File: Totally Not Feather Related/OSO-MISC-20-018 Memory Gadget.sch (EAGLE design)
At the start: 57 parts, among them IC1 LS013B4DN04, IC2 S-882150APH, IC3 ATSAMD21G18_QFN, J2 10118193-0001LF, J4 SM04B-SRSS-TB(LF)(SN), Q1 DMG341, SW1 JS102011SAQN, SW2 SPST_TACT-KMR2, U1 MCP73831T-2ACI/OT, U2 AP2112K-3.3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

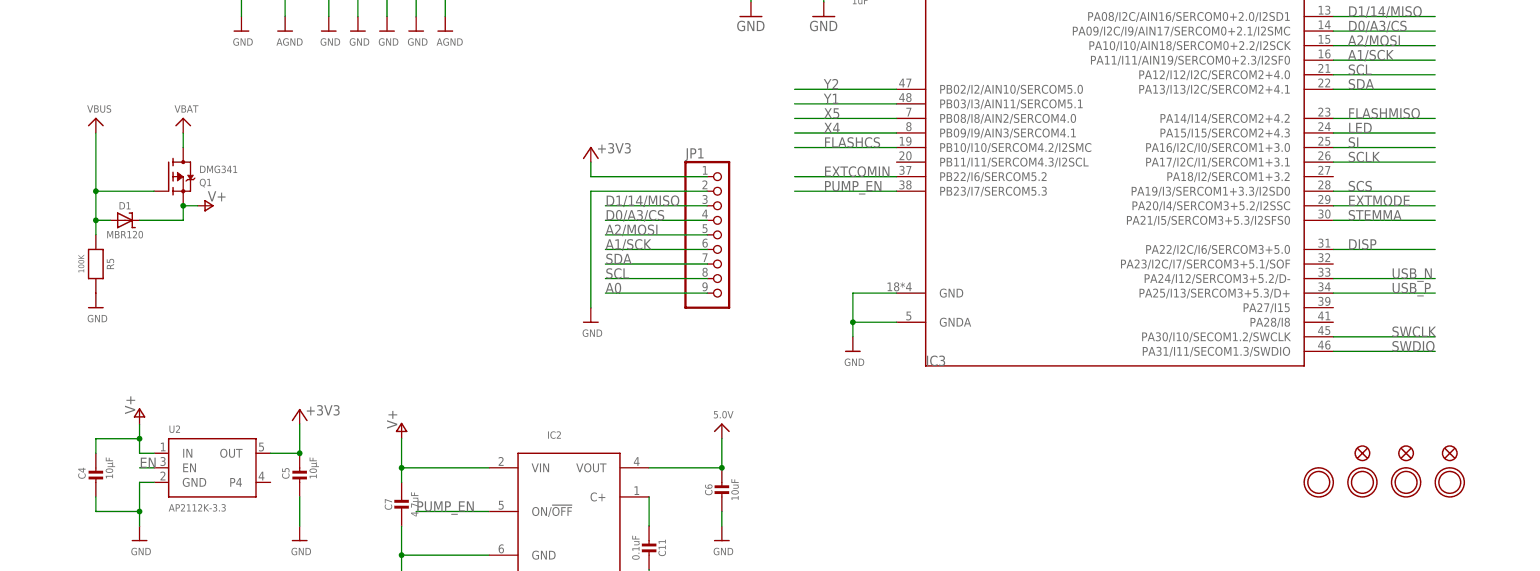
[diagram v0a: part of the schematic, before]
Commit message: add EN pull-up, fix SPI flash pin selection
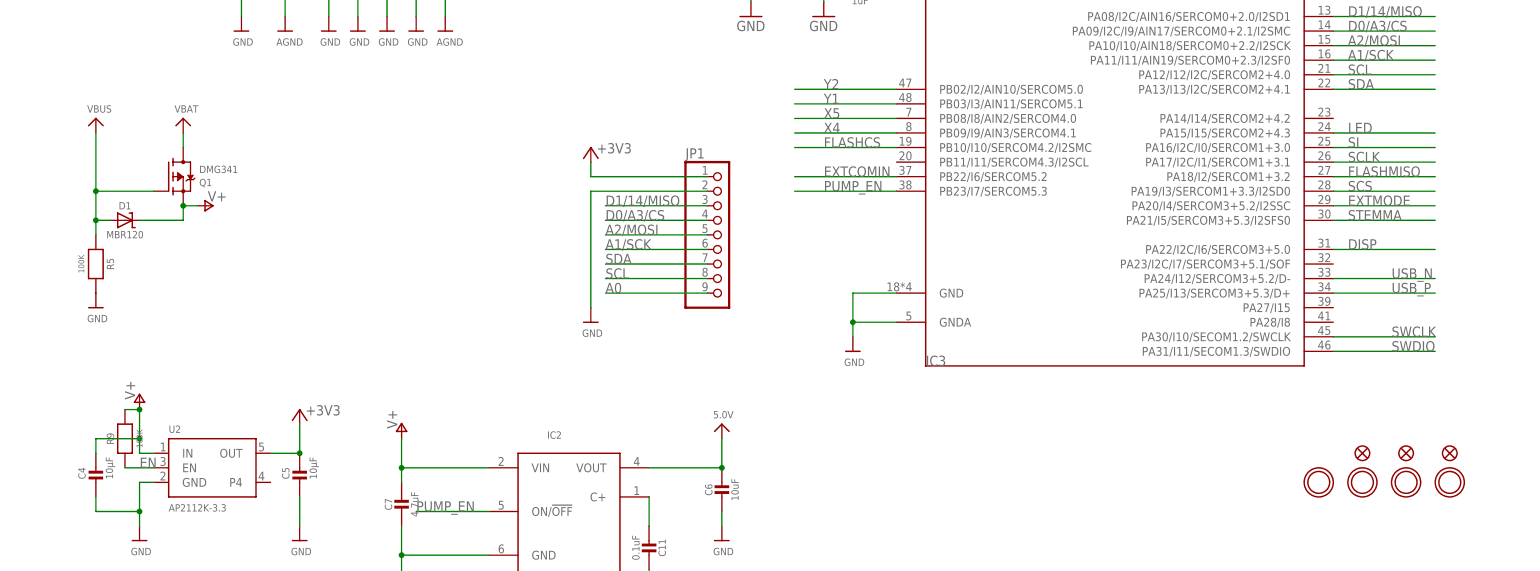
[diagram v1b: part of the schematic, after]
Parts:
- added R9: 100K, microbuilder:RESISTOR0805_NOOUTLINE
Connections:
- net EN: now also R9.1
- net FLASHMISO: now also IC3.PA18/I2/SERCOM1+3.2; no longer IC3.PA14/I14/SERCOM2+4.2
- net V+: now also R9.2
